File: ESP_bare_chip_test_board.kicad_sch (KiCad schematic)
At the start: 0 parts

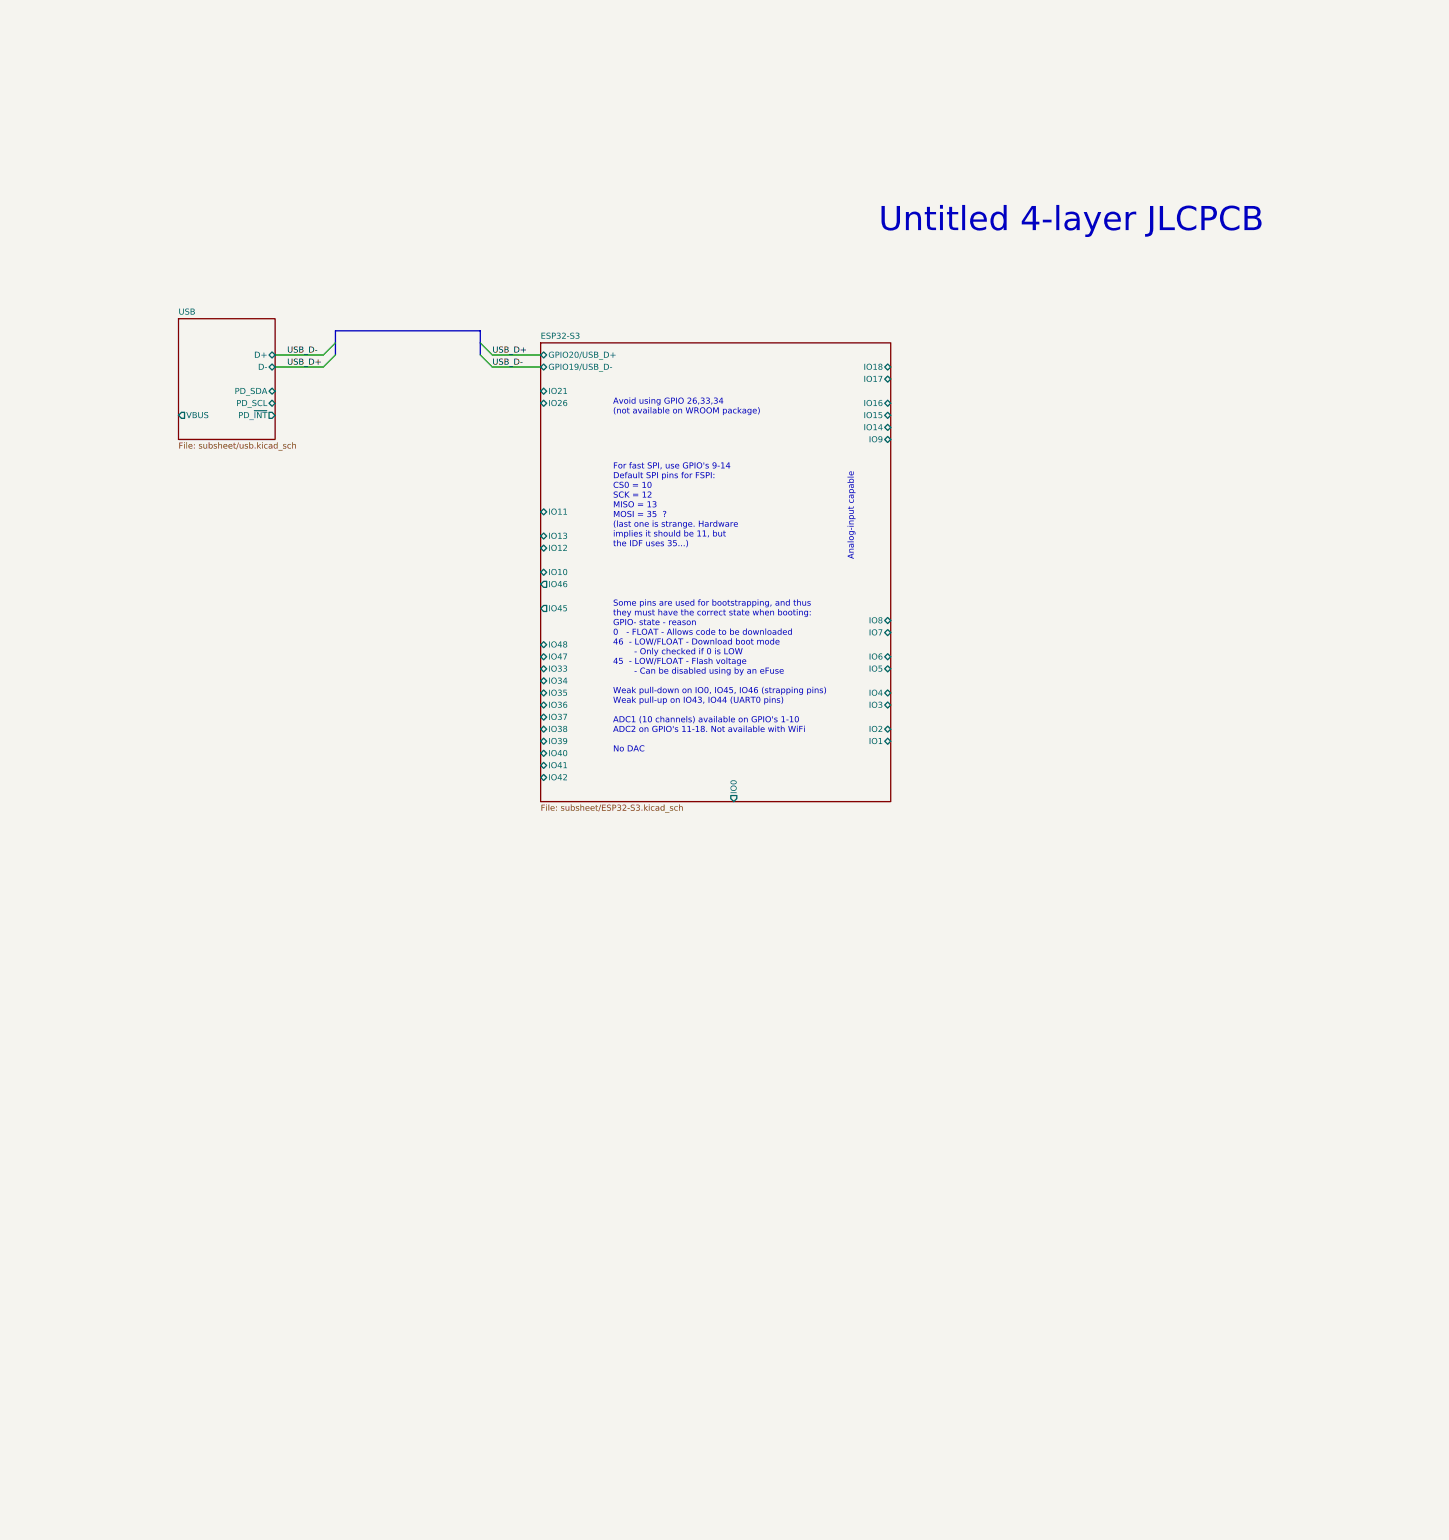
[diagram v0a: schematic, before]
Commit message: Update file format to KiCAD 8.0.0
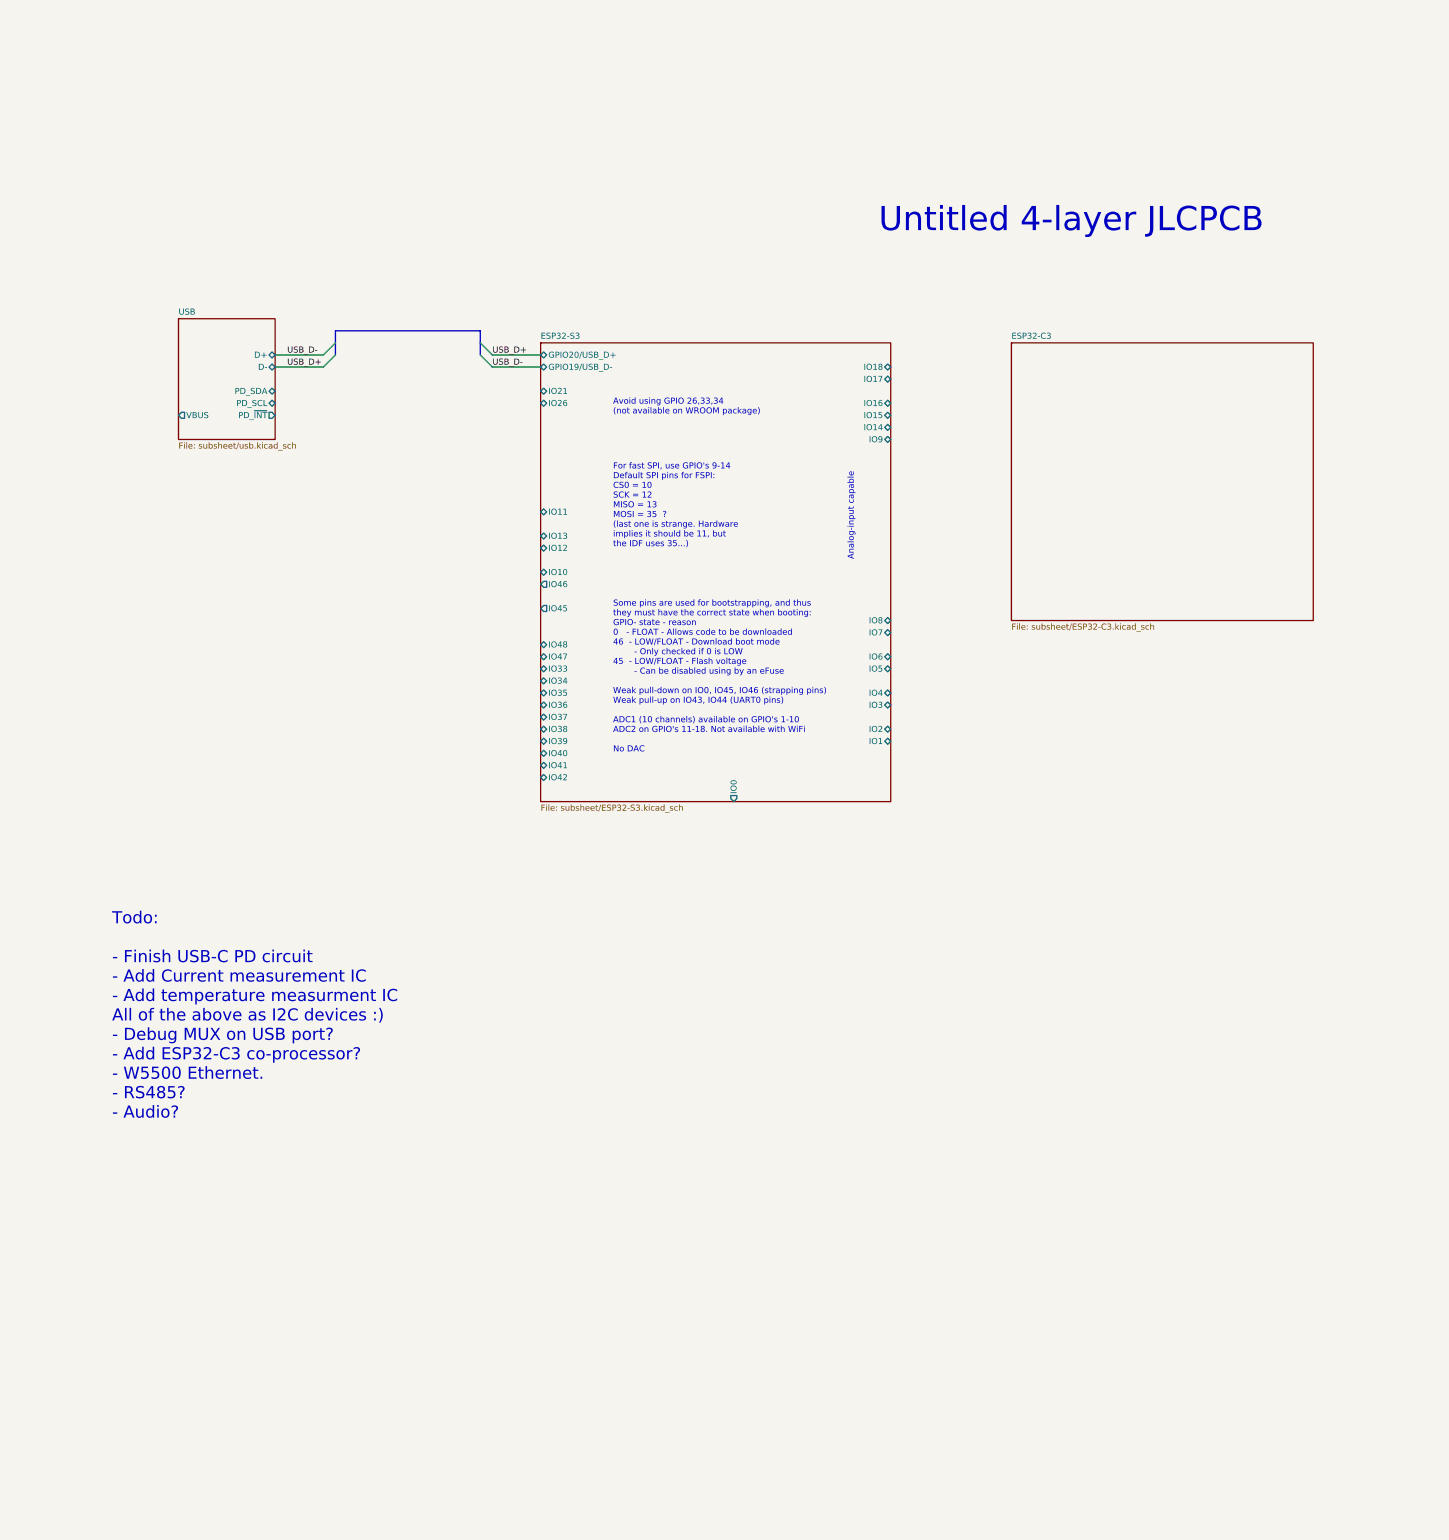
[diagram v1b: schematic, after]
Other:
- added sheet ESP32-C3 (subsheet/ESP32-C3.kicad_sch)
- note added: "Todo: - Finish USB-C PD circuit - Add Current measurement IC - Add temperature measurment IC All of the above as I2C devices :) - Debug MUX on USB port? - Add ESP32-C3 co-processor? - W5500 Ethernet. - RS485? - Audio?"

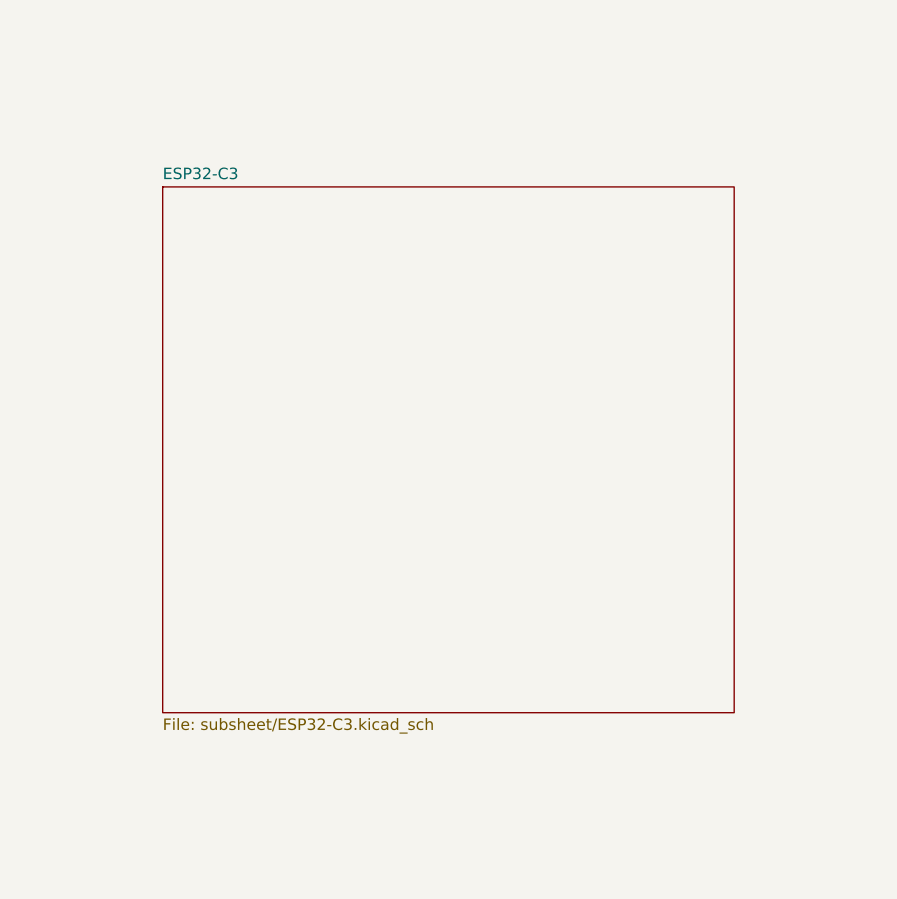
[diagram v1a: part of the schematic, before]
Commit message: Add ESP32-C3 subsheet. SMall corrections
Add and wire up ESP32-C3-Mini on a subsheet, and note down which pins
are used for strapping etc. This will then be replaced with a bare-chip
ESP32-C3 circuit, much like with the existing ESP32-S3 circuit.
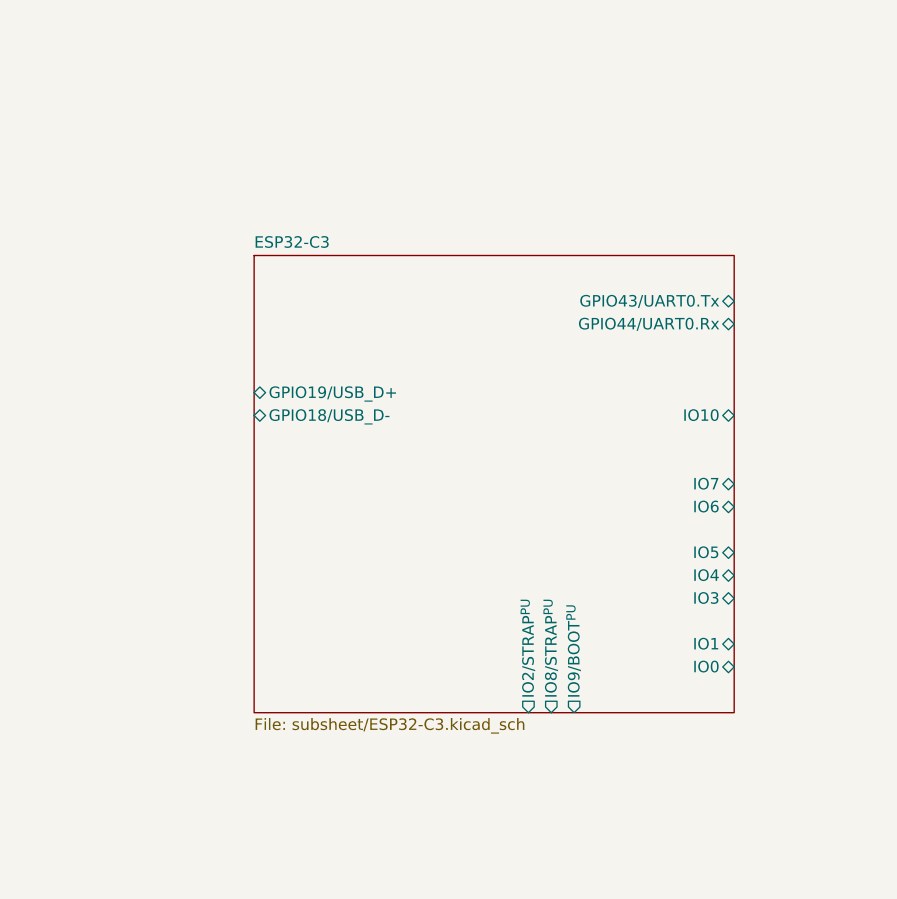
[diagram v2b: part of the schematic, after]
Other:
- sheet ESP32-C3 ports: added GPIO18/USB_D-, GPIO19/USB_D+, GPIO43/UART0.Tx, GPIO44/UART0.Rx, IO0, IO1, IO10, IO2/STRAP^{PU}, IO3, IO4, IO5, IO6, IO7, IO8/STRAP^{PU}, IO9/BOOT^{PU}; removed none
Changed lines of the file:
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@@
 	)
 	(sheet
-		(at 208.28 30.48)
-		(size 63.5 58.42)
+		(at 218.44 38.1)
+		(size 53.34 50.8)
 		(fields_autoplaced yes)
 		(stroke
@@
 		)
 		(property "Sheetname" "ESP32-C3"
-			(at 208.28 29.7684 0)
+			(at 218.44 37.3884 0)
 			(effects
 				(font
@@
 		)
 		(property "Sheetfile" "subsheet/ESP32-C3.kicad_sch"
-			(at 208.28 89.4846 0)
+			(at 218.44 89.4846 0)
 			(effects
 				(font
@@
 			)
 		)
+		(pin "GPIO18{slash}USB_D-" bidirectional
+			(at 218.44 55.88 180)
+			(effects
+				(font
+					(size 1.27 1.27)
+				)
+				(justify left)
+			)
+		)
+		(pin "GPIO19{slash}USB_D+" bidirectional
+			(at 218.44 53.34 180)
+			(effects
+				(font
+					(size 1.27 1.27)
+				)
+				(justify left)
+			)
+		)
+		(pin "IO1" bidirectional
+			(at 271.78 81.28 0)
+			(effects
+				(font
+					(size 1.27 1.27)
+				)
+				(justify right)
+			)
+		)
+		(pin "IO0" bidirectional
+			(at 271.78 83.82 0)
+			(effects
+				(font
+					(size 1.27 1.27)
+				)
+				(justify right)
+			)
+		)
+		(pin "IO5" bidirectional
+			(at 271.78 71.12 0)
+			(effects
+				(font
+					(size 1.27 1.27)
+				)
+				(justify right)
+			)
+		)
+		(pin "IO3" bidirectional
+			(at 271.78 76.2 0)
+			(effects
+				(font
+					(size 1.27 1.27)
+				)
+				(justify right)
+			)
+		)
+		(pin "IO4" bidirectional
+			(at 271.78 73.66 0)
+			(effects
+				(font
+					(size 1.27 1.27)
+				)
+				(justify right)
+			)
+		)
+		(pin "IO6" bidirectional
+			(at 271.78 66.04 0)
+			(effects
+				(font
+					(size 1.27 1.27)
+				)
+				(justify right)
+			)
+		)
+		(pin "GPIO44{slash}UART0.Rx" bidirectional
+			(at 271.78 45.72 0)
+			(effects
+				(font
+					(size 1.27 1.27)
+				)
+				(justify right)
+			)
+		)
+		(pin "GPIO43{slash}UART0.Tx" bidirectional
+			(at 271.78 43.18 0)
+			(effects
+				(font
+					(size 1.27 1.27)
+				)
+				(justify right)
+			)
+		)
+		(pin "IO8{slash}STRAP^{PU}" output
+			(at 251.46 88.9 270)
+			(effects
+				(font
+					(size 1.27 1.27)
+				)
+				(justify left)
+			)
+		)
+		(pin "IO9{slash}BOOT^{PU}" output
+			(at 254 88.9 270)
+			(effects
+				(font
+					(size 1.27 1.27)
+				)
+				(justify left)
+			)
+		)
+		(pin "IO2{slash}STRAP^{PU}" output
+			(at 248.92 88.9 270)
+			(effects
+				(font
+					(size 1.27 1.27)
+				)
+				(justify left)
+			)
+		)
+		(pin "IO7" bidirectional
+			(at 271.78 63.5 0)
+			(effects
+				(font
+					(size 1.27 1.27)
+				)
+				(justify right)
+			)
+		)
+		(pin "IO10" bidirectional
+			(at 271.78 55.88 0)
+			(effects
+				(font
+					(size 1.27 1.27)
+				)
+				(justify right)
+			)
+		)
